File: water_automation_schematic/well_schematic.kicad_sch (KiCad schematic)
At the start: 1 part, among them U1 lolin32_lite_V1.00

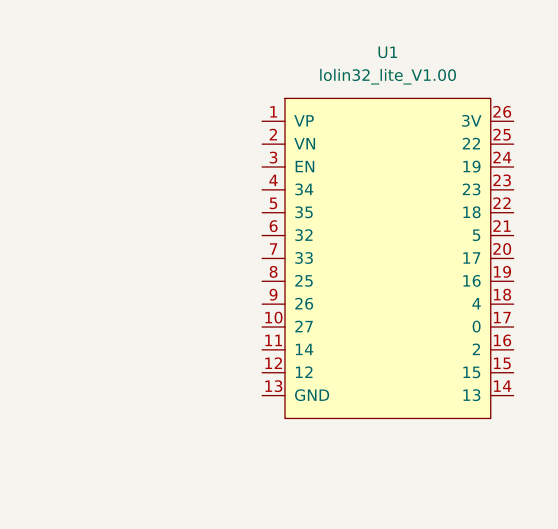
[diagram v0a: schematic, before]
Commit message: added us sensor logic
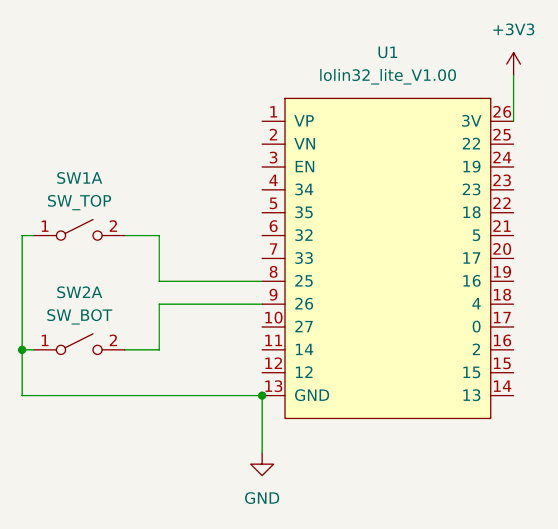
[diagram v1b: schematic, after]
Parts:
- added SW1: SW_TOP, symbol Switch:SW_DPST_x2
- added SW2: SW_BOT, symbol Switch:SW_DPST_x2
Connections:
- net GND: now reaches U1.13 (GND)
- net GND: now also SW1.1 (A), SW2.1 (A)
- net +3V3: now reaches U1.26 (3V)
- net at U1.8 (25): now also SW1.2 (B)
- net at U1.9 (26): now also SW2.2 (B)
